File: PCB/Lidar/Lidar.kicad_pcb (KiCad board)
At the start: 2 copper layers, 22.9 x 30.5 mm, 3 parts, among them P16 LIDAR_LEFT, P17 CONN_02X03, P18 LIDAR_RIGHT

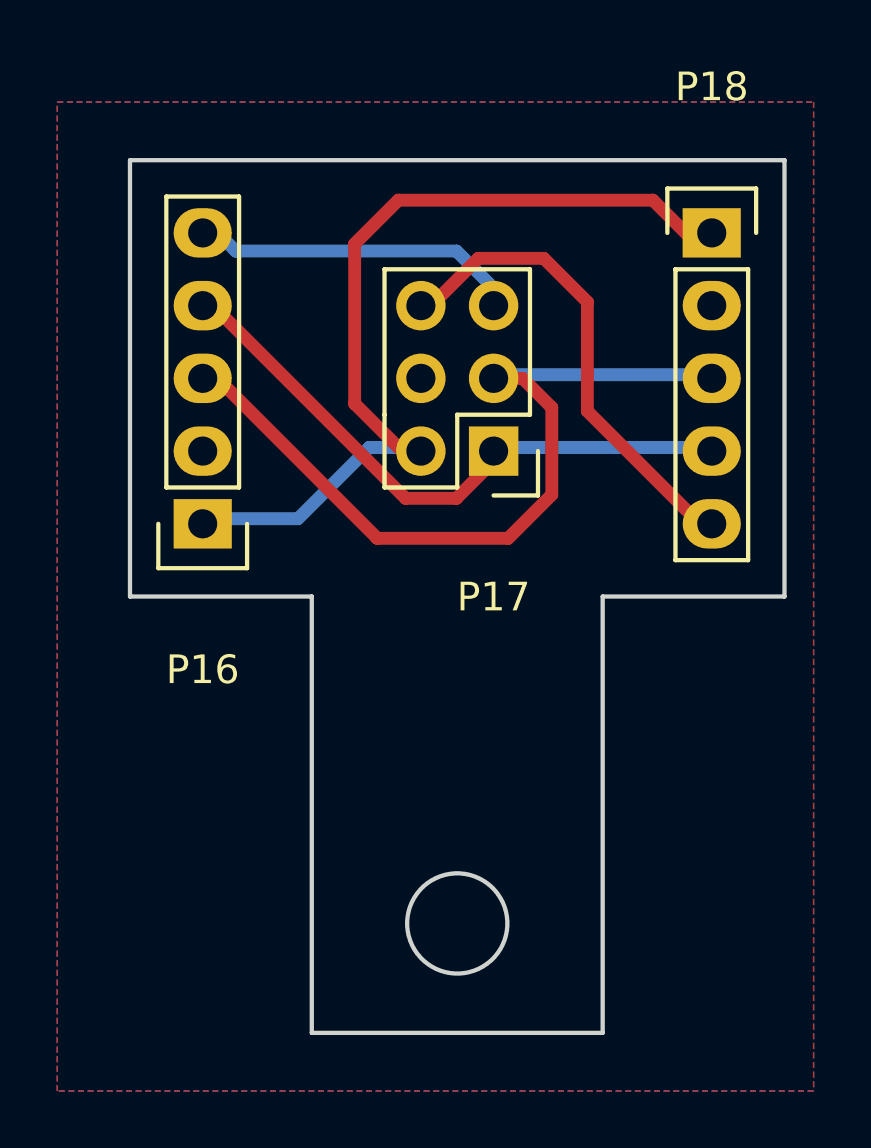
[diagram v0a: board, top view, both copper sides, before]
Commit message: Improve:  Lidar PCB silk
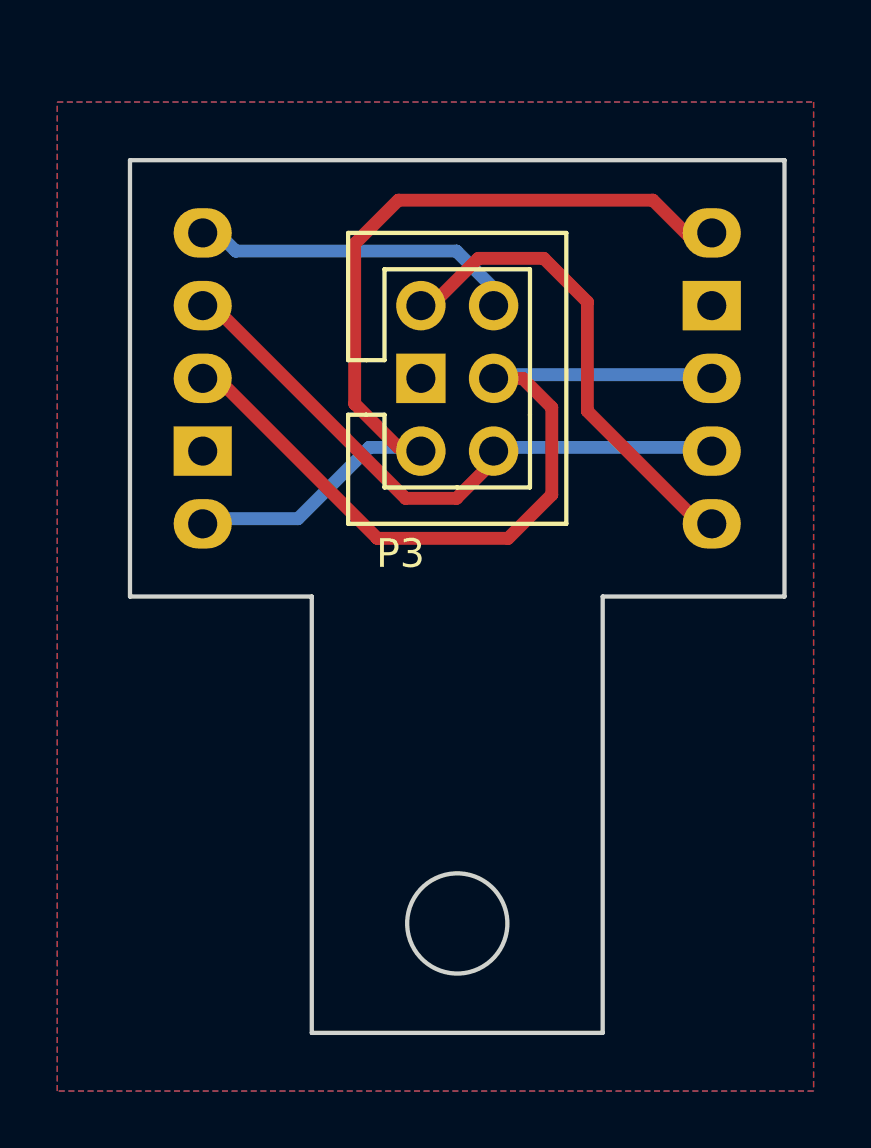
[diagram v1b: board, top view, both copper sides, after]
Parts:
- renumbered P16 to P1, P18 to P2, P17 to P3
